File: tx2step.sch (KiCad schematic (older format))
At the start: 38 parts, among them IC1 ATMEGA328P-MM

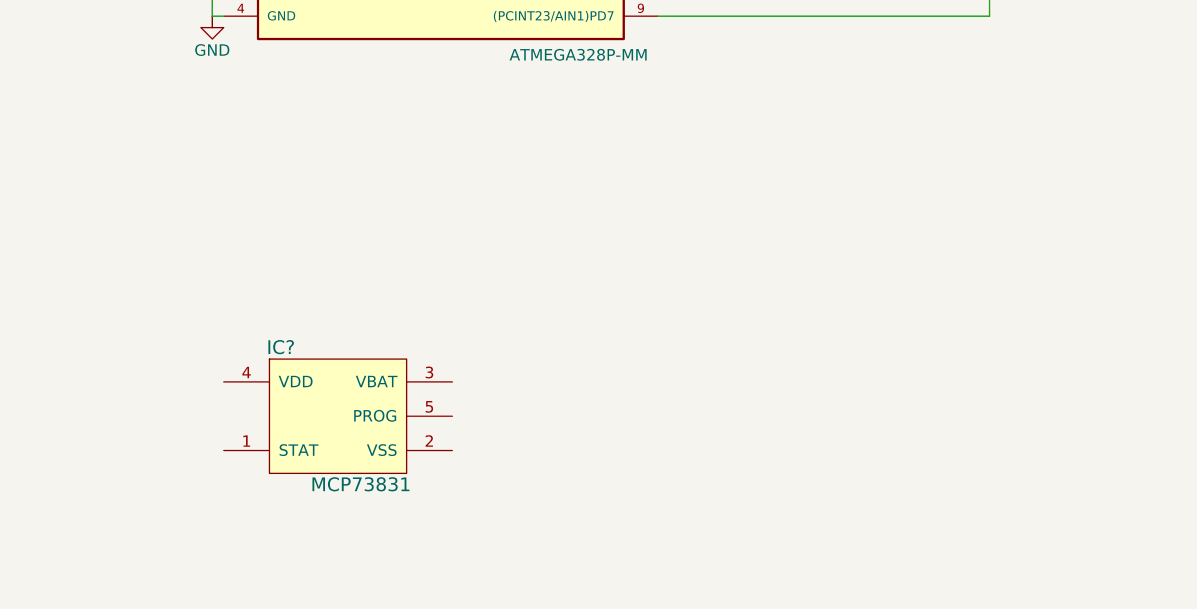
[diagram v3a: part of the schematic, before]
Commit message: Add additional power ICs
TPS2113A power multiplexer and TPS61202 boost converter.
Not wired up yet.
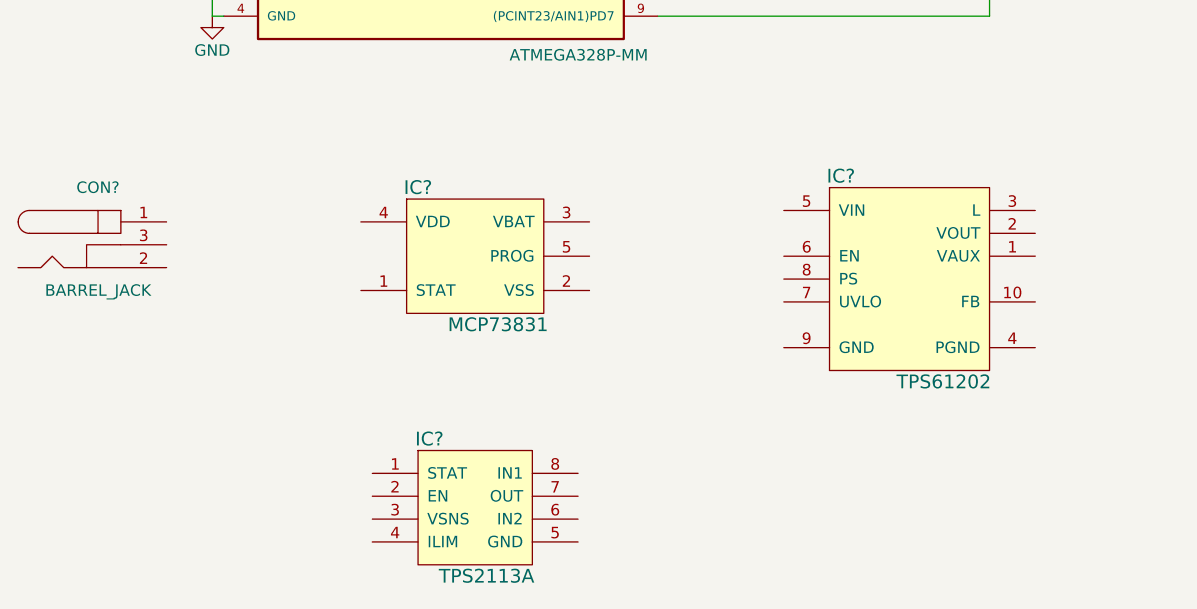
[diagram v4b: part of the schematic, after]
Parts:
- added CON?: BARREL_JACK, symbol BARREL_JACK
- added IC?: TPS61202, symbol TPS61202
- added IC?: TPS2113A, symbol TPS2113A
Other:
- moved on the sheet: IC?
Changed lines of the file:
@@
 L MCP73831 IC?
 U 1 1 58B862EA
-P 2050 6950
-F 0 "IC?" H 1800 7250 60  0000 C CNN
-F 1 "MCP73831" H 2150 6650 60  0000 C CNN
-F 2 "" H 1800 7250 60  0001 C CNN
-F 3 "" H 1800 7250 60  0001 C CNN
-	1    2050 6950
+P 2650 6250
+F 0 "IC?" H 2400 6550 60  0000 C CNN
+F 1 "MCP73831" H 2750 5950 60  0000 C CNN
+F 2 "" H 2400 6550 60  0001 C CNN
+F 3 "" H 2400 6550 60  0001 C CNN
+	1    2650 6250
 	1    0    0    -1
 $EndComp
@@
 Wire Wire Line
 	8850 2750 8850 2850
+$Comp
+L TPS61202 IC?
+U 1 1 58BACDA2
+P 4550 6350
+F 0 "IC?" H 4250 6800 60  0000 C CNN
+F 1 "TPS61202" H 4700 5900 60  0000 C CNN
+F 2 "" H 4300 6850 60  0001 C CNN
+F 3 "" H 4300 6850 60  0001 C CNN
+	1    4550 6350
+	1    0    0    -1
+$EndComp
+$Comp
+L TPS2113A IC?
+U 1 1 58BAD11D
+P 2650 7350
+F 0 "IC?" H 2450 7650 60  0000 C CNN
+F 1 "TPS2113A" H 2700 7050 60  0000 C CNN
+F 2 "" H 2300 7800 60  0001 C CNN
+F 3 "" H 2300 7800 60  0001 C CNN
+	1    2650 7350
+	1    0    0    -1
+$EndComp
+$Comp
+L BARREL_JACK CON?
+U 1 1 58BAF2CD
+P 1000 6200
+F 0 "CON?" H 1000 6450 50  0000 C CNN
+F 1 "BARREL_JACK" H 1000 6000 50  0000 C CNN
+F 2 "" H 1000 6200 50  0000 C CNN
+F 3 "" H 1000 6200 50  0000 C CNN
+	1    1000 6200
+	1    0    0    -1
+$EndComp
 $EndSCHEMATC

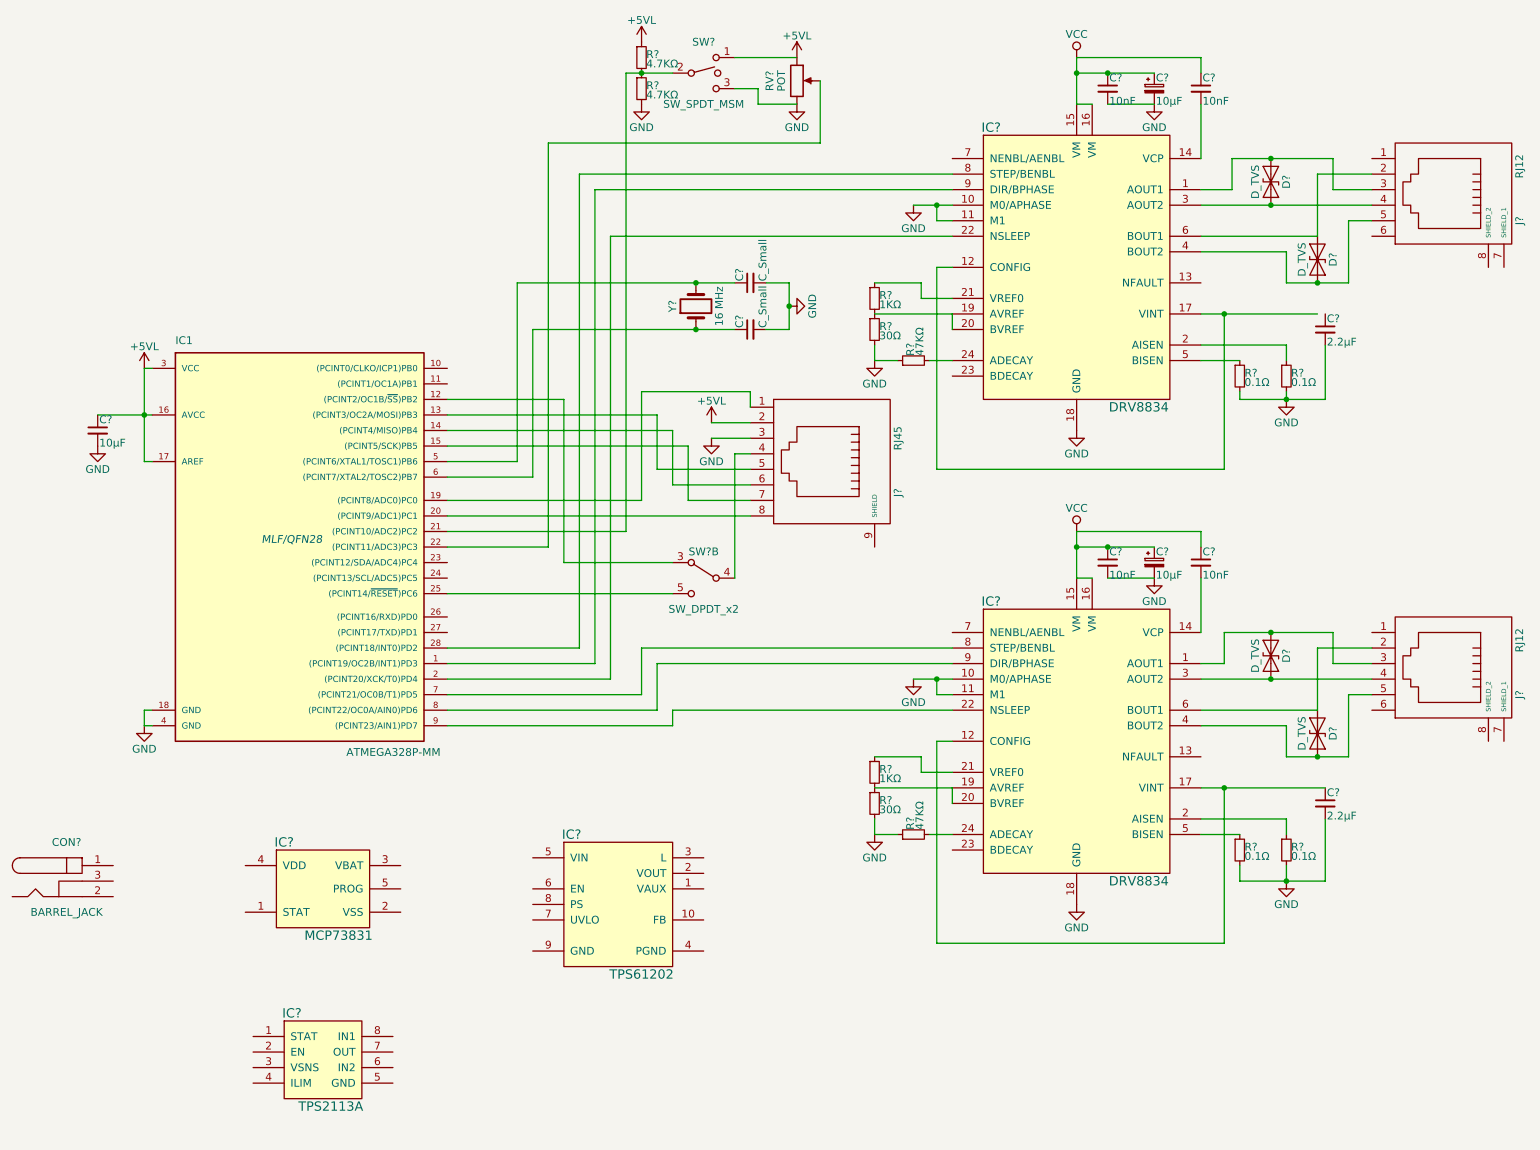
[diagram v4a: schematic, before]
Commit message: Connect MCP73831 and battery
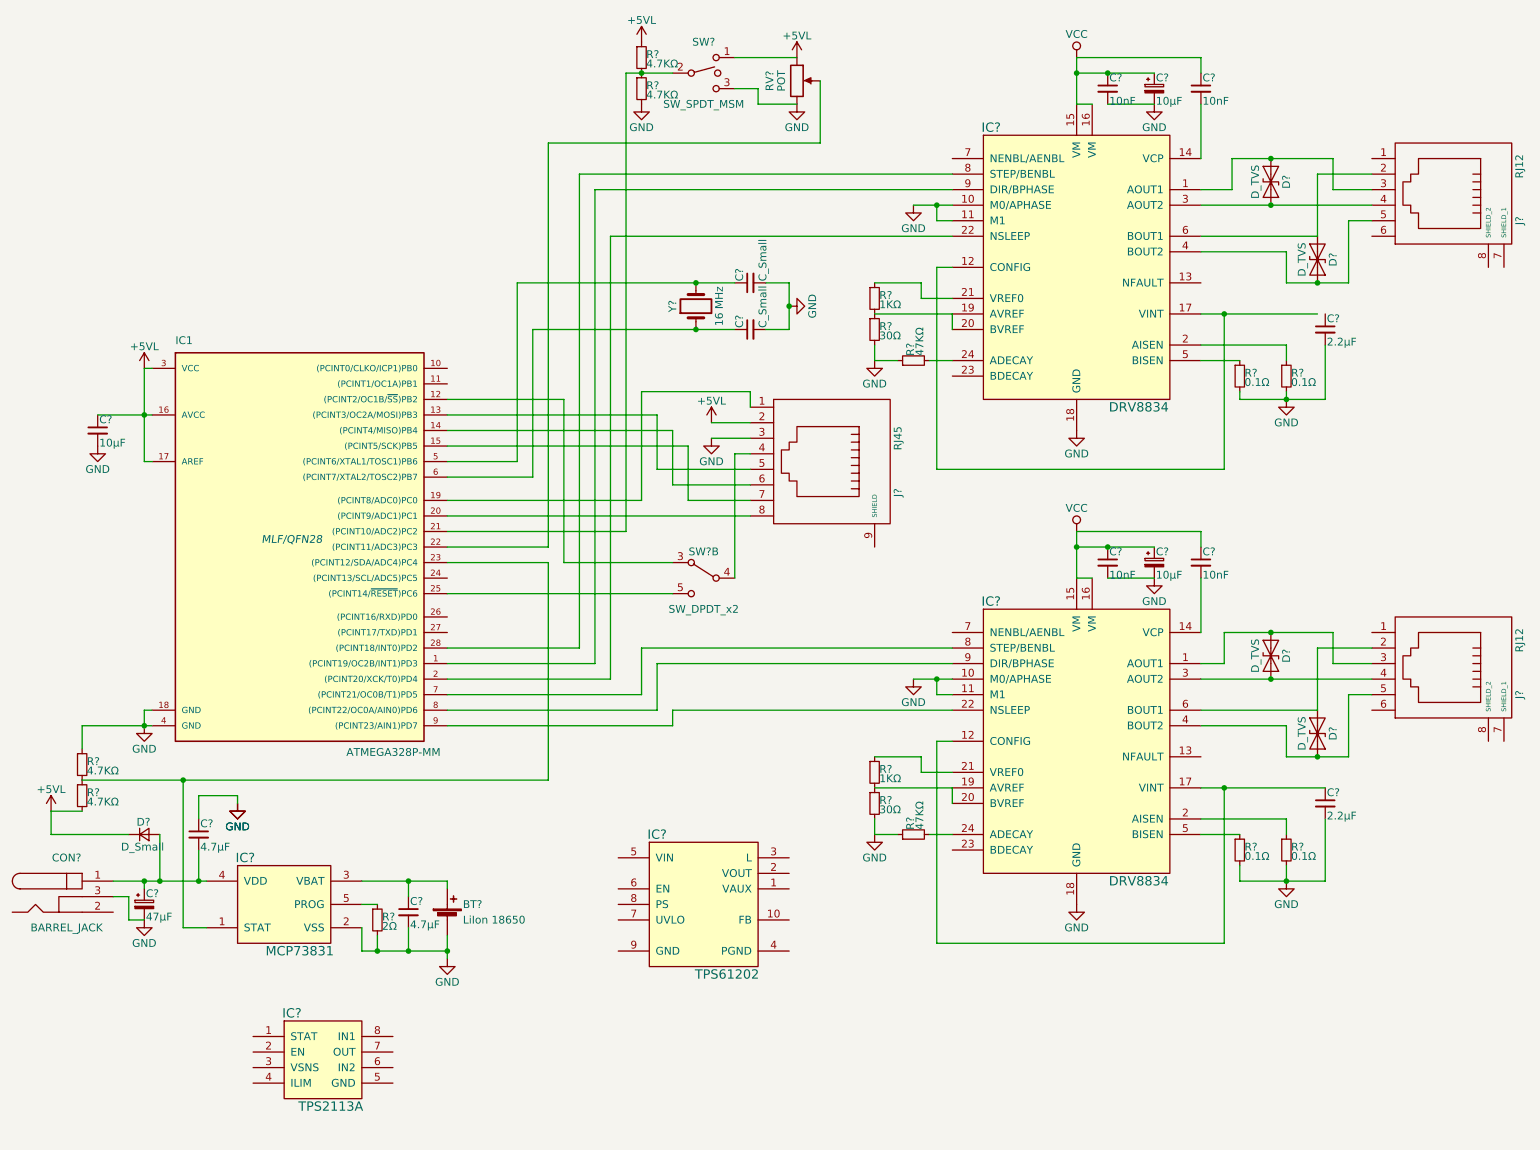
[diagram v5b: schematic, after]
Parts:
- added BT?: LiIon 18650, symbol Battery_Cell
- added C?: 47µF, symbol CP_Small
- added C? (x2): 4.7µF, symbol C_Small
- added D?: D_Small, symbol D_Small
- added R? (x2): 4.7KΩ, symbol R_Small
- added R?: 2Ω, symbol R_Small
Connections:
- net +5VL: now also D?.1 (K), R?.2
- net GND: now also CON?.3, IC?.2 (VSS), BT?.2 (-), C?.1, C?.2, C?.2, R?.1, R?.2
- net at IC1.23 ((PCINT12/SDA/ADC4)PC4): now also IC?.1 (STAT), R?.1, R?.2
- net at IC?.3 (VBAT): now also BT?.1 (+), C?.1
- net at IC?.4 (VDD): now also CON?.1, C?.1, C?.2, D?.2 (A)
- net at IC?.5 (PROG): now also R?.1
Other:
- moved on the sheet: CON?, IC?

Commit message: Connect DC in and battery to multiplexer
The DC in source will take priority. Also connect the charge state LED.
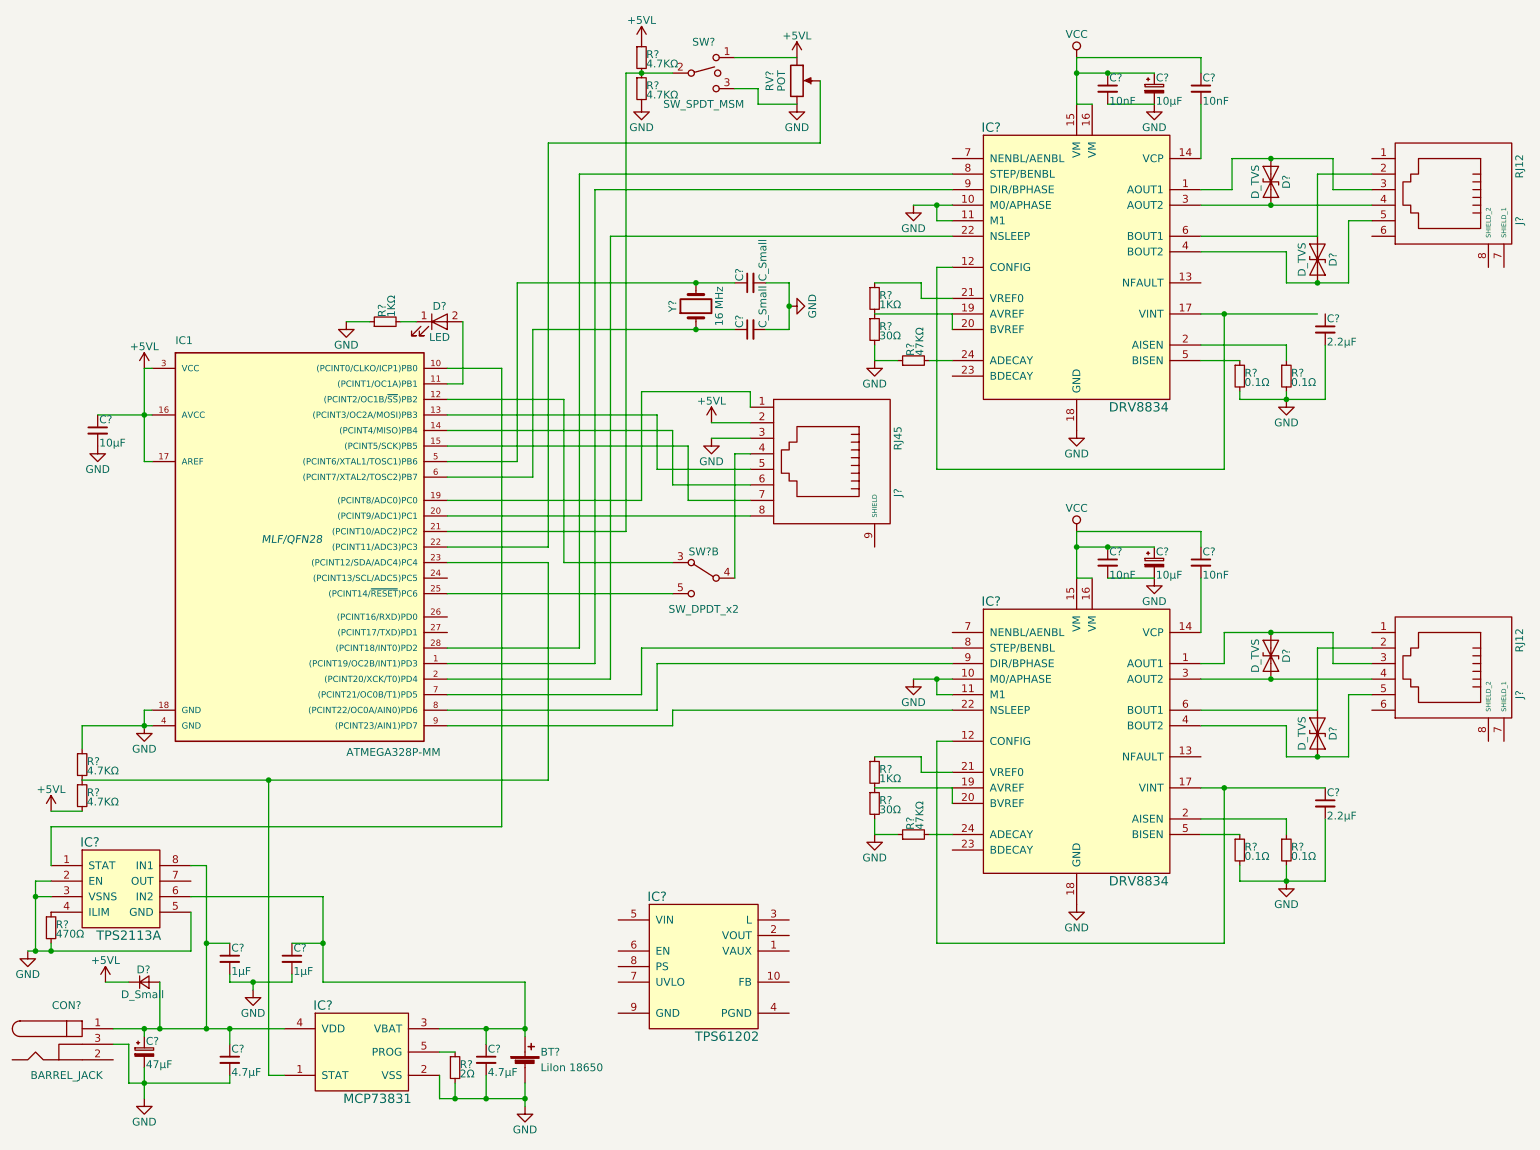
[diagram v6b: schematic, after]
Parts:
- added C? (x2): 1µF, symbol C_Small
- added D?: LED, symbol LED
- added R?: 470Ω, symbol R_Small
- added R?: 1KΩ, symbol R_Small
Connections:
- net GND: now also C?.2, IC?.2 (EN), IC?.3 (VSNS), IC?.5 (GND), C?.2, C?.2, R?.1, R?.2; no longer C?.1
- net at IC1.10 ((PCINT0/CLKO/ICP1)PB0): now also IC?.1 (STAT)
- net at IC1.11 ((PCINT1/OC1A)PB1): now also D?.2 (A)
- net at BT?.1 (+), C?.1, IC?.3 (VBAT): now also IC?.6 (IN2), C?.1
- net at C?.1, CON?.1, D?.2 (A)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: now also C?.1, IC?.8 (IN1), C?.1; no longer C?.2
- net at IC?.4 (ILIM): now also R?.1
- new net: D?.1 (K), R?.2
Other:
- moved on the sheet: BT?, C?, CON?, D?, IC?, R?

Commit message: Separate DC power from power area of schematic
This makes it a little cleaner and easier to visualize the relationship
between the DC in source and the logic/main voltage rails.
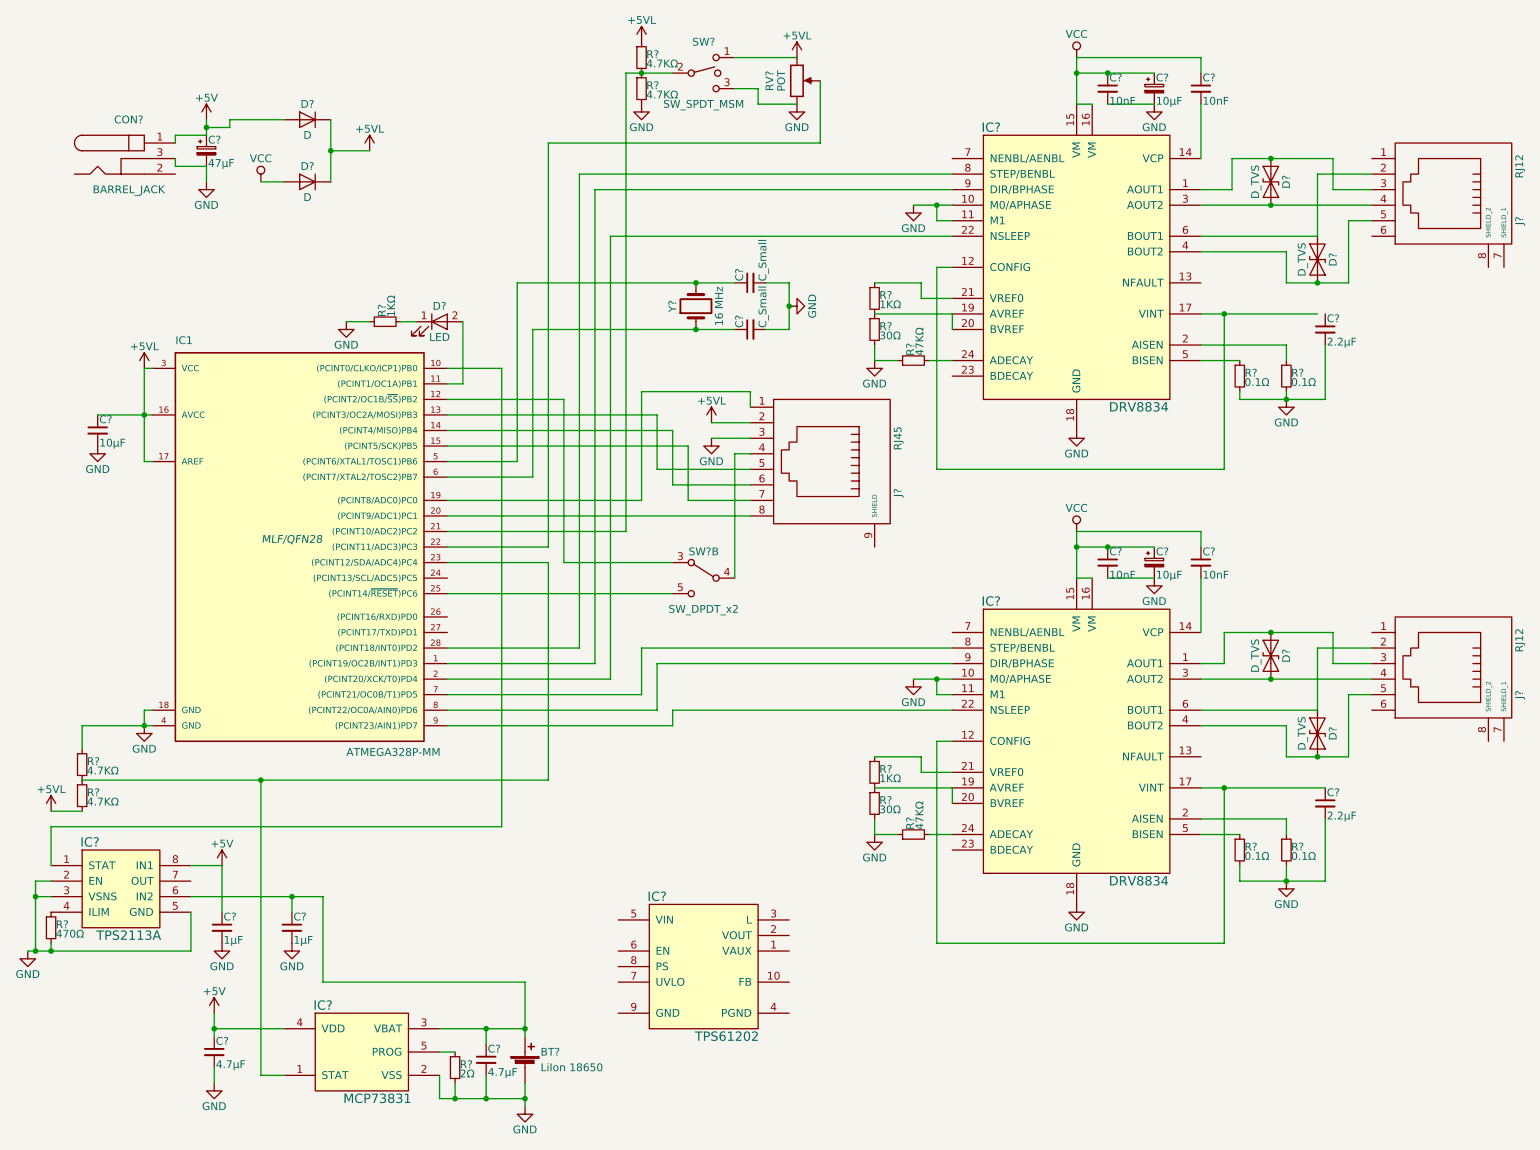
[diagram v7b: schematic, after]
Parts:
- removed D?: D_Small, symbol D_Small
- added D? (x2): D, symbol D
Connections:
- net +5VL: now also D?.1 (K), D?.1 (K)
- net VCC: now also D?.2 (A)
- net +5V: now reaches C?.1, C?.1, C?.1, CON?.1, IC?.4 (VDD), IC?.8 (IN1)
- net +5V: now also D?.2 (A)
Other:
- moved on the sheet: C?, CON?
